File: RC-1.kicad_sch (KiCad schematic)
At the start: 0 parts

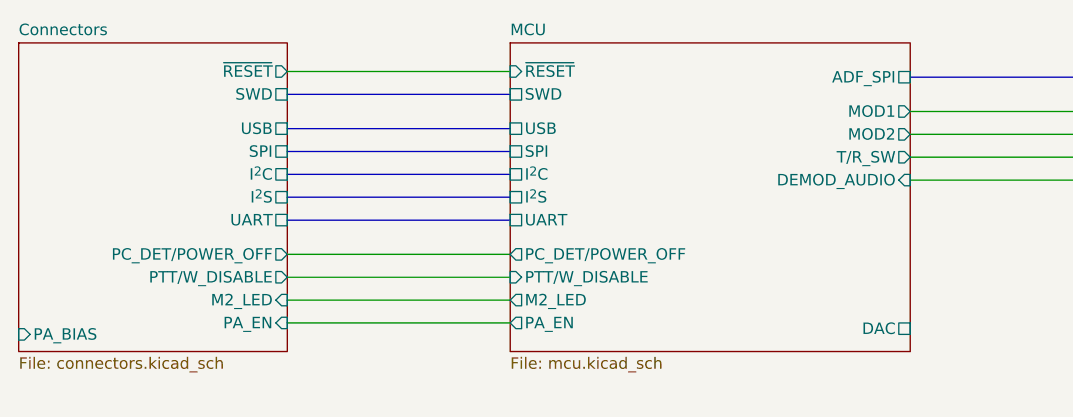
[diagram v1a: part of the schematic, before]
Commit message: Split PC_DETECT and POWER_OFF lines
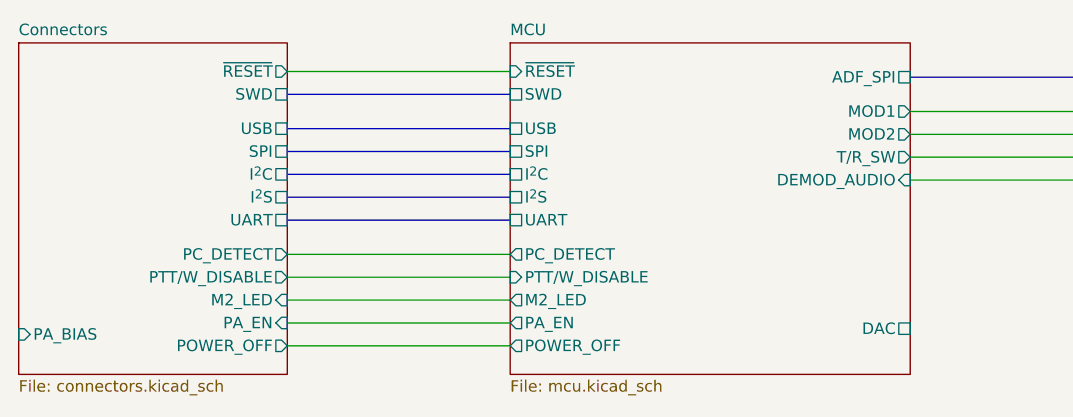
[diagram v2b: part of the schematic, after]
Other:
- sheet Connectors ports: added PC_DETECT, POWER_OFF; removed PC_DET/POWER_OFF
- sheet MCU ports: added PC_DETECT, POWER_OFF; removed PC_DET/POWER_OFF
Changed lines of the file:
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@@
     (company "OpenRTX + M17")
   )
+  (wire (pts (xy 106.045 114.935) (xy 130.81 114.935))
+    (stroke (width 0) (type default) (color 0 0 0 0))
+  )
   (wire (pts (xy 106.045 109.855) (xy 130.81 109.855))
     (stroke (width 0) (type default) (color 0 0 0 0))
@@
     (stroke (width 0) (type default) (color 0 0 0 0))
   )
-  (sheet (at 130.81 81.28) (size 44.45 34.29) (fields_autoplaced)
+  (sheet (at 130.81 81.28) (size 44.45 36.83) (fields_autoplaced)
     (stroke (width 0.1524) (type solid) (color 0 0 0 0))
     (fill (color 0 0 0 0.0000))
@@
       (effects (font (size 1.27 1.27)) (justify left bottom))
     )
-    (property "Sheet file" "mcu.kicad_sch" (id 1) (at 130.81 116.1546 0)
+    (property "Sheet file" "mcu.kicad_sch" (id 1) (at 130.81 118.6946 0)
       (effects (font (size 1.27 1.27)) (justify left top))
     )
@@
       (effects (font (size 1.27 1.27)) (justify left))
     )
-    (pin "PC_DET{slash}POWER_OFF" output (at 130.81 104.775 180)
-      (effects (font (size 1.27 1.27)) (justify left))
-    )
     (pin "I^{2}C" passive (at 130.81 95.885 180)
       (effects (font (size 1.27 1.27)) (justify left))
@@
       (effects (font (size 1.27 1.27)) (justify left))
     )
-  )
-  (sheet (at 76.2 81.28) (size 29.845 34.29) (fields_autoplaced)
+    (pin "PC_DETECT" output (at 130.81 104.775 180)
+      (effects (font (size 1.27 1.27)) (justify left))
+    )
+    (pin "POWER_OFF" output (at 130.81 114.935 180)
+      (effects (font (size 1.27 1.27)) (justify left))
+    )
+  )
+  (sheet (at 76.2 81.28) (size 29.845 36.83) (fields_autoplaced)
     (stroke (width 0.1524) (type solid) (color 0 0 0 0))
     (fill (color 0 0 0 0.0000))
@@
       (effects (font (size 1.27 1.27)) (justify left bottom))
     )
-    (property "Sheet file" "connectors.kicad_sch" (id 1) (at 76.2 116.1546 0)
+    (property "Sheet file" "connectors.kicad_sch" (id 1) (at 76.2 118.6946 0)
       (effects (font (size 1.27 1.27)) (justify left top))
     )
@@
       (effects (font (size 1.27 1.27)) (justify right))
     )
-    (pin "PC_DET{slash}POWER_OFF" output (at 106.045 104.775 0)
-      (effects (font (size 1.27 1.27)) (justify right))
-    )
     (pin "M2_LED" input (at 106.045 109.855 0)
       (effects (font (size 1.27 1.27)) (justify right))
     )
     (pin "I^{2}S" passive (at 106.045 98.425 0)
+      (effects (font (size 1.27 1.27)) (justify right))
+    )
+    (pin "PC_DETECT" output (at 106.045 104.775 0)
+      (effects (font (size 1.27 1.27)) (justify right))
+    )
+    (pin "POWER_OFF" output (at 106.045 114.935 0)
       (effects (font (size 1.27 1.27)) (justify right))
     )
@@
       (reference "#PWR?") (unit 1) (value "GND") (footprint "")
     )
-    (path "/d054b6a0-3a84-4aaa-901c-78f33fd51c3e/24d96d92-0033-41bb-b7f6-17c401a56838"
-      (reference "#PWR?") (unit 1) (value "GND") (footprint "")
-    )
     (path "/e9b5eb9e-a5da-44ea-89cf-1dbc5f8707b1/2a6a8c96-9ee1-43a6-969f-063b295c4901"
       (reference "#PWR?") (unit 1) (value "GND") (footprint "")
@@
       (reference "#PWR?") (unit 1) (value "+3V3") (footprint "")
     )
+    (path "/d054b6a0-3a84-4aaa-901c-78f33fd51c3e/78705ef4-849b-40e4-a931-27dc787ae8c9"
+      (reference "#PWR?") (unit 1) (value "+3V3") (footprint "")
+    )
     (path "/e9b5eb9e-a5da-44ea-89cf-1dbc5f8707b1/8026b4e0-e17a-4cb6-ba47-0bad44d9bba2"
       (reference "#PWR?") (unit 1) (value "GND") (footprint "")
@@
       (reference "R?") (unit 1) (value "100k") (footprint "Resistor_SMD:R_0402_1005Metric")
     )
+    (path "/d054b6a0-3a84-4aaa-901c-78f33fd51c3e/52101c5f-8443-4303-bf5c-ab8d0ac553b3"
+      (reference "R?") (unit 1) (value "100k") (footprint "Resistor_SMD:R_0402_1005Metric")
+    )
     (path "/37f64190-0af6-4571-a391-bfca4fb830ce/57b03ce9-6a2c-4f8c-926f-8d19ed2a8dd3"
       (reference "R?") (unit 1) (value "10k") (footprint "")
@@
       (reference "R?") (unit 1) (value "270") (footprint "Resistor_SMD:R_0402_1005Metric")
     )
-    (path "/d054b6a0-3a84-4aaa-901c-78f33fd51c3e/66b6219f-e4e9-460a-9a48-80326a41b79d"
-      (reference "R?") (unit 1) (value "100k") (footprint "Resistor_SMD:R_0402_1005Metric")
-    )
     (path "/e9b5eb9e-a5da-44ea-89cf-1dbc5f8707b1/6d137e50-4f3c-48f7-b67a-04e4af16e7bc"

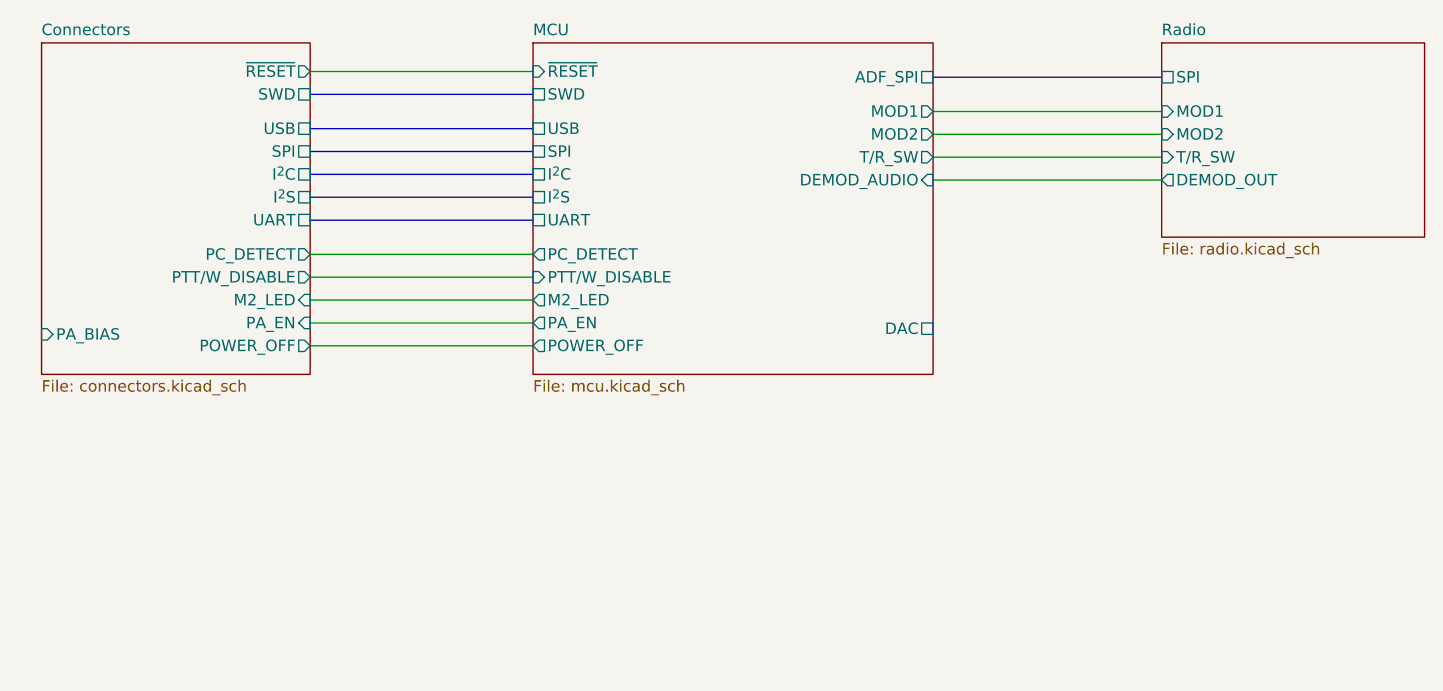
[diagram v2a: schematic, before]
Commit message: Connected ADF7021 chip enable to MCU, grouped PTT/W_DISABLE signal with SWDIO
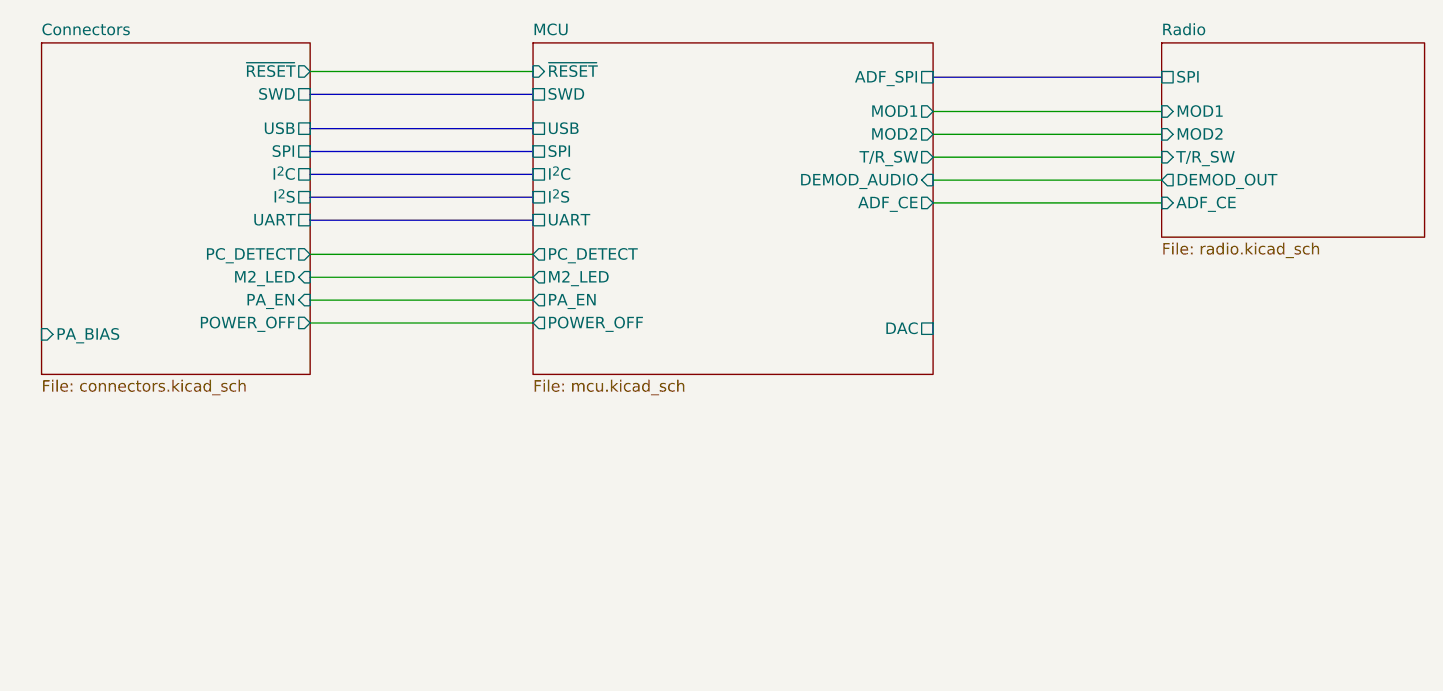
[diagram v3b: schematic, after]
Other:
- sheet Connectors ports: added none; removed PTT/W_DISABLE
- sheet MCU ports: added ADF_CE; removed PTT/W_DISABLE
- sheet Radio ports: added ADF_CE; removed none
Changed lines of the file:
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@@
     (company "OpenRTX + M17")
   )
-  (wire (pts (xy 106.045 114.935) (xy 130.81 114.935))
+  (wire (pts (xy 106.045 112.395) (xy 130.81 112.395))
+    (stroke (width 0) (type default) (color 0 0 0 0))
+  )
+  (wire (pts (xy 106.045 107.315) (xy 130.81 107.315))
     (stroke (width 0) (type default) (color 0 0 0 0))
   )
@@
     (stroke (width 0) (type default) (color 0 0 0 0))
   )
-  (wire (pts (xy 106.045 112.395) (xy 130.81 112.395))
-    (stroke (width 0) (type default) (color 0 0 0 0))
-  )
   (bus (pts (xy 106.045 95.885) (xy 130.81 95.885))
     (stroke (width 0) (type default) (color 0 0 0 0))
@@
     (stroke (width 0) (type default) (color 0 0 0 0))
   )
+  (wire (pts (xy 175.26 99.06) (xy 200.66 99.06))
+    (stroke (width 0) (type default) (color 0 0 0 0))
+  )
   (wire (pts (xy 175.26 88.9) (xy 200.66 88.9))
     (stroke (width 0) (type default) (color 0 0 0 0))
@@
   )
   (wire (pts (xy 106.045 84.455) (xy 130.81 84.455))
-    (stroke (width 0) (type default) (color 0 0 0 0))
-  )
-  (wire (pts (xy 106.045 107.315) (xy 130.81 107.315))
     (stroke (width 0) (type default) (color 0 0 0 0))
   )
@@
       (effects (font (size 1.27 1.27)) (justify right))
     )
-    (pin "M2_LED" output (at 130.81 109.855 180)
+    (pin "M2_LED" output (at 130.81 107.315 180)
       (effects (font (size 1.27 1.27)) (justify left))
     )
@@
       (effects (font (size 1.27 1.27)) (justify right))
     )
-    (pin "PA_EN" output (at 130.81 112.395 180)
+    (pin "PA_EN" output (at 130.81 109.855 180)
       (effects (font (size 1.27 1.27)) (justify left))
     )
@@
       (effects (font (size 1.27 1.27)) (justify right))
     )
-    (pin "PTT{slash}W_DISABLE" input (at 130.81 107.315 180)
-      (effects (font (size 1.27 1.27)) (justify left))
-    )
     (pin "DAC" passive (at 175.26 113.03 0)
       (effects (font (size 1.27 1.27)) (justify right))
@@
       (effects (font (size 1.27 1.27)) (justify left))
     )
-    (pin "POWER_OFF" output (at 130.81 114.935 180)
-      (effects (font (size 1.27 1.27)) (justify left))
+    (pin "POWER_OFF" output (at 130.81 112.395 180)
+      (effects (font (size 1.27 1.27)) (justify left))
+    )
+    (pin "ADF_CE" output (at 175.26 99.06 0)
+      (effects (font (size 1.27 1.27)) (justify right))
     )
   )
@@
       (effects (font (size 1.27 1.27)) (justify right))
     )
-    (pin "PA_EN" input (at 106.045 112.395 0)
+    (pin "PA_EN" input (at 106.045 109.855 0)
       (effects (font (size 1.27 1.27)) (justify right))
     )
@@
       (effects (font (size 1.27 1.27)) (justify right))
     )
-    (pin "PTT{slash}W_DISABLE" output (at 106.045 107.315 0)
-      (effects (font (size 1.27 1.27)) (justify right))
-    )
-    (pin "M2_LED" input (at 106.045 109.855 0)
+    (pin "M2_LED" input (at 106.045 107.315 0)
       (effects (font (size 1.27 1.27)) (justify right))
     )
@@
       (effects (font (size 1.27 1.27)) (justify right))
     )
-    (pin "POWER_OFF" output (at 106.045 114.935 0)
+    (pin "POWER_OFF" output (at 106.045 112.395 0)
       (effects (font (size 1.27 1.27)) (justify right))
     )
@@
       (effects (font (size 1.27 1.27)) (justify left))
     )
+    (pin "ADF_CE" input (at 200.66 99.06 180)
+      (effects (font (size 1.27 1.27)) (justify left))
+    )
   )
   (sheet_instances
@@
       (reference "#PWR?") (unit 1) (value "GND") (footprint "")
     )
+    (path "/e9b5eb9e-a5da-44ea-89cf-1dbc5f8707b1/321442de-1be8-447c-864f-6a257a7c6538"
+      (reference "#PWR?") (unit 1) (value "GND") (footprint "")
+    )
     (path "/e9b5eb9e-a5da-44ea-89cf-1dbc5f8707b1/3c355365-ccea-4f26-982b-cada0c513c82"
       (reference "#PWR?") (unit 1) (value "GND") (footprint "")
@@
       (reference "R?") (unit 1) (value "100") (footprint "Resistor_SMD:R_0402_1005Metric")
     )
+    (path "/e9b5eb9e-a5da-44ea-89cf-1dbc5f8707b1/888ac178-64f7-43b4-b707-72fcc082fe7f"
+      (reference "R?") (unit 1) (value "10k") (footprint "Resistor_SMD:R_0402_1005Metric")
+    )
     (path "/d054b6a0-3a84-4aaa-901c-78f33fd51c3e/892c2ce4-3701-4250-accf-fd778c33b016"

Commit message: Added I2C for external EEPROM on the M.2 connector, added pull-up resistors on the I2C lines
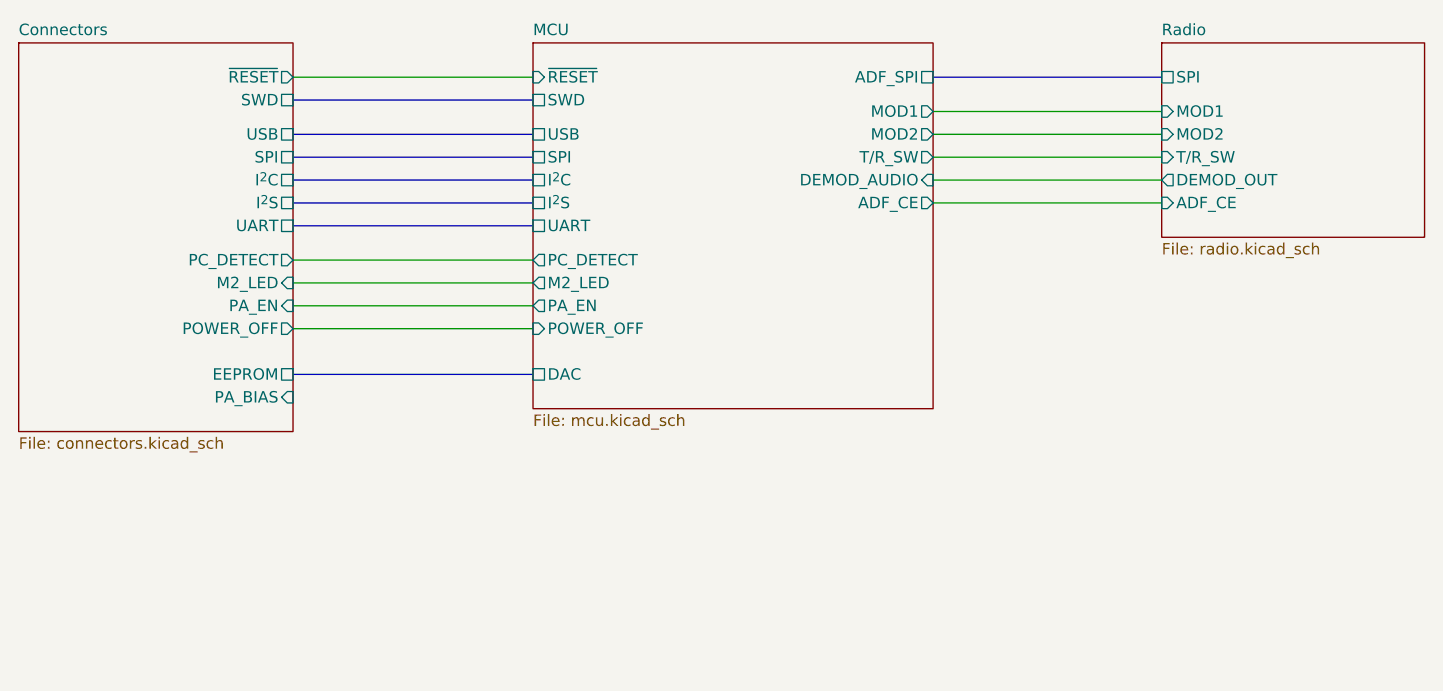
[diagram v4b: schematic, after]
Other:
- sheet Connectors ports: added EEPROM; removed none
